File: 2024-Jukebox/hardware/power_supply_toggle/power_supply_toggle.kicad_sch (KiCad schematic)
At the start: 6 parts, among them J1 Conn_01x02, J2 Conn_01x02, J3 Conn_01x02, U1 74HC74

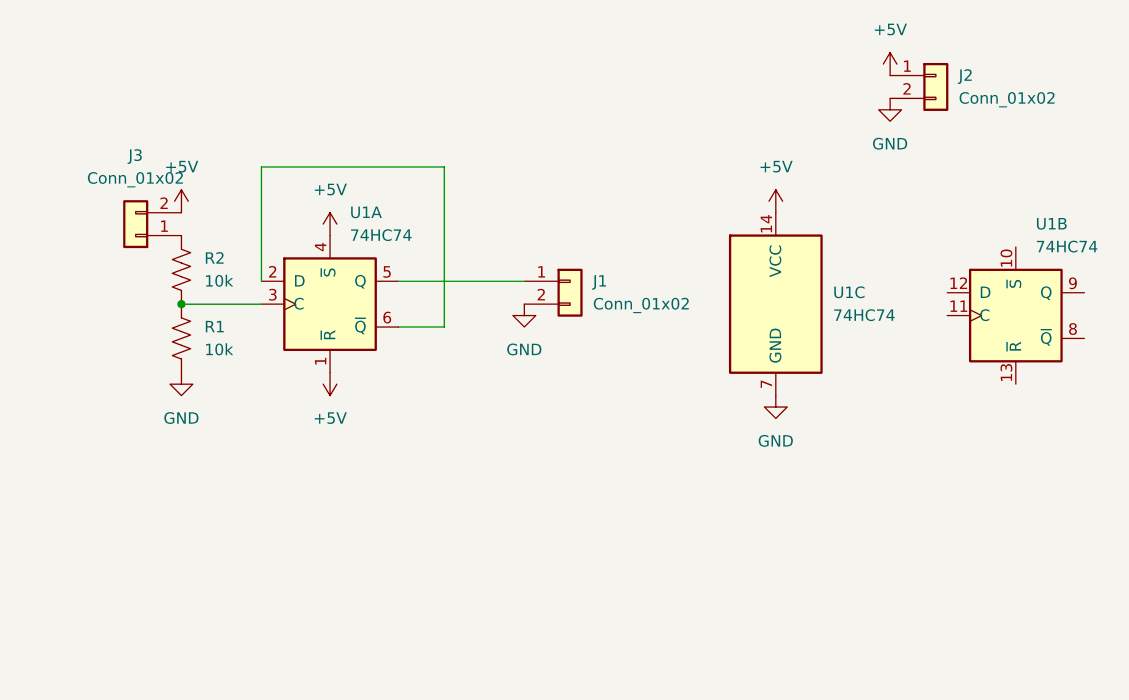
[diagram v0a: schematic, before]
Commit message: Added decoupling cap to power supply toggle board
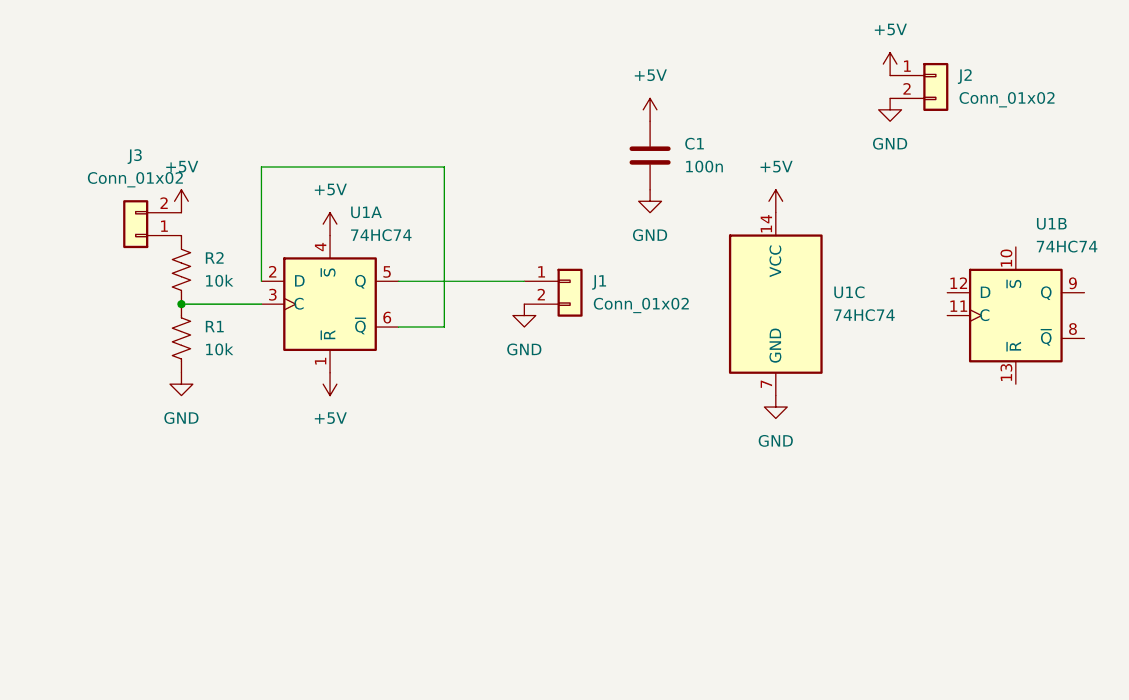
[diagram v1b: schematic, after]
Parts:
- added C1: 100n, Capacitor_SMD:C_0603_1608Metric, symbol Device:C
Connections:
- net +5V: now also C1.1
- net GND: now also C1.2
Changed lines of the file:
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@@
+    )
+  )
+  (symbol (lib_id "Device:C") (at 138.43 34.29 0) (unit 1)
+    (in_bom yes) (on_board yes) (dnp no) (fields_autoplaced)
+    (property "Reference" "C1" (at 142.24 33.02 0)
+      (effects (font (size 1.27 1.27)) (justify left))
+    )
+    (property "Value" "100n" (at 142.24 35.56 0)
+      (effects (font (size 1.27 1.27)) (justify left))
+    )
+    (property "Footprint" "Capacitor_SMD:C_0603_1608Metric" (at 139.3952 38.1 0)
+      (effects (font (size 1.27 1.27)) hide)
+    )
+    (property "Datasheet" "~" (at 138.43 34.29 0)
+      (effects (font (size 1.27 1.27)) hide)
+    )
+    (pin "1")
+    (pin "2")
+    (instances
+      (project "power_supply_toggle"
+        (path "/a273dd55-31a1-4938-9db8-9ea089537404"
+          (reference "C1") (unit 1)
+        )
+      )
     )
   )
@@
         (path "/a273dd55-31a1-4938-9db8-9ea089537404"
           (reference "#PWR02") (unit 1)
+        )
+      )
+    )
+  )
+  (symbol (lib_id "power:GND") (at 138.43 38.1 0) (unit 1)
+    (in_bom yes) (on_board yes) (dnp no) (fields_autoplaced)
+    (property "Reference" "#PWR011" (at 138.43 44.45 0)
+      (effects (font (size 1.27 1.27)) hide)
+    )
+    (property "Value" "GND" (at 138.43 43.18 0)
+      (effects (font (size 1.27 1.27)))
+    )
+    (property "Footprint" "" (at 138.43 38.1 0)
+      (effects (font (size 1.27 1.27)) hide)
+    )
+    (property "Datasheet" "" (at 138.43 38.1 0)
+      (effects (font (size 1.27 1.27)) hide)
+    )
+    (pin "1")
+    (instances
+      (project "power_supply_toggle"
+        (path "/a273dd55-31a1-4938-9db8-9ea089537404"
+          (reference "#PWR011") (unit 1)
         )
       )
@@
         )
       )
+    )
+  )
+  (symbol (lib_id "power:+5V") (at 138.43 30.48 0) (unit 1)
+    (in_bom yes) (on_board yes) (dnp no) (fields_autoplaced)
+    (property "Reference" "#PWR010" (at 138.43 34.29 0)
+      (effects (font (size 1.27 1.27)) hide)
+    )
+    (property "Value" "+5V" (at 138.43 25.4 0)
+      (effects (font (size 1.27 1.27)))
+    )
+    (property "Footprint" "" (at 138.43 30.48 0)
+      (effects (font (size 1.27 1.27)) hide)
+    )
+    (property "Datasheet" "" (at 138.43 30.48 0)
+      (effects (font (size 1.27 1.27)) hide)
+    )
+    (pin "1")
+    (instances
+      (project "power_supply_toggle"
+        (path "/a273dd55-31a1-4938-9db8-9ea089537404"
+          (reference "#PWR010") (unit 1)
+        )
+      )

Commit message: Updated power supply toggle pcb
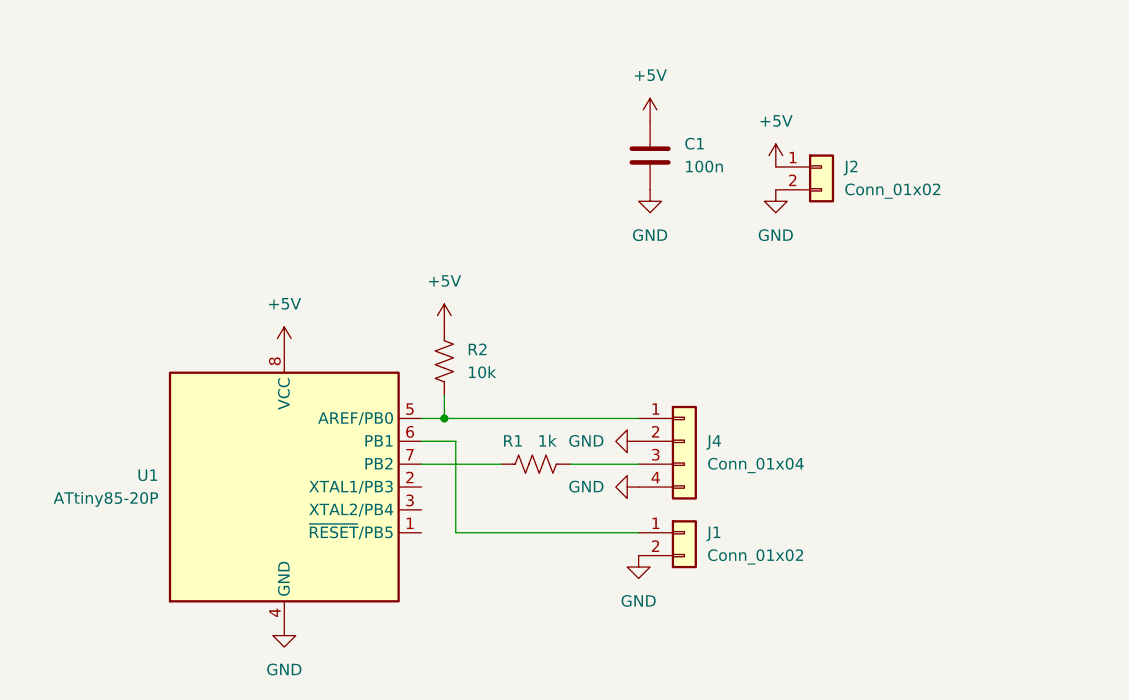
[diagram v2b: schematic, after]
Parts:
- removed J3: Conn_01x02, Connector_PinHeader_2.54mm:PinHeader_1x02_P2.54mm_Vertical, symbol Connector_Generic:Conn_01x02
- removed U1: 74HC74, Package_DIP:DIP-14_W7.62mm, symbol 74xx:74HC74
- added J4: Conn_01x04, Connector_JST:JST_XH_B4B-XH-A_1x04_P2.50mm_Vertical, symbol Connector_Generic:Conn_01x04
- added U1: ATtiny85-20P, Package_DIP:DIP-8_W7.62mm, symbol MCU_Microchip_ATtiny:ATtiny85-20P
- R1: value 10k -> 1k
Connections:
- net +5V: now also R2.1, U1.8 (VCC)
- net GND: now also J4.2 (Pin_2), J4.4 (Pin_4), U1.4 (GND); no longer R1.2
- net at J1.1 (Pin_1): now also U1.6 (PB1)
- net at R1.1: now also U1.7 (PB2); no longer R2.2
- new net: J4.3 (Pin_3), R1.2
- new net: J4.1 (Pin_1), R2.2, U1.5 (AREF/PB0)
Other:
- moved on the sheet: J1, J2, R2
